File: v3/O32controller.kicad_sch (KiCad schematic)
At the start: 43 parts, among them J1 BATT+, J2 BATT+, J3 BATT-, J4 BATT-, J5 NTC, J6 SWD, J7 ExternalSPI, J8 RS485, J9 RS485, U1 STSPIN32F0ATR, U2 THVD1420DRLR, U3 MA702GQ-P

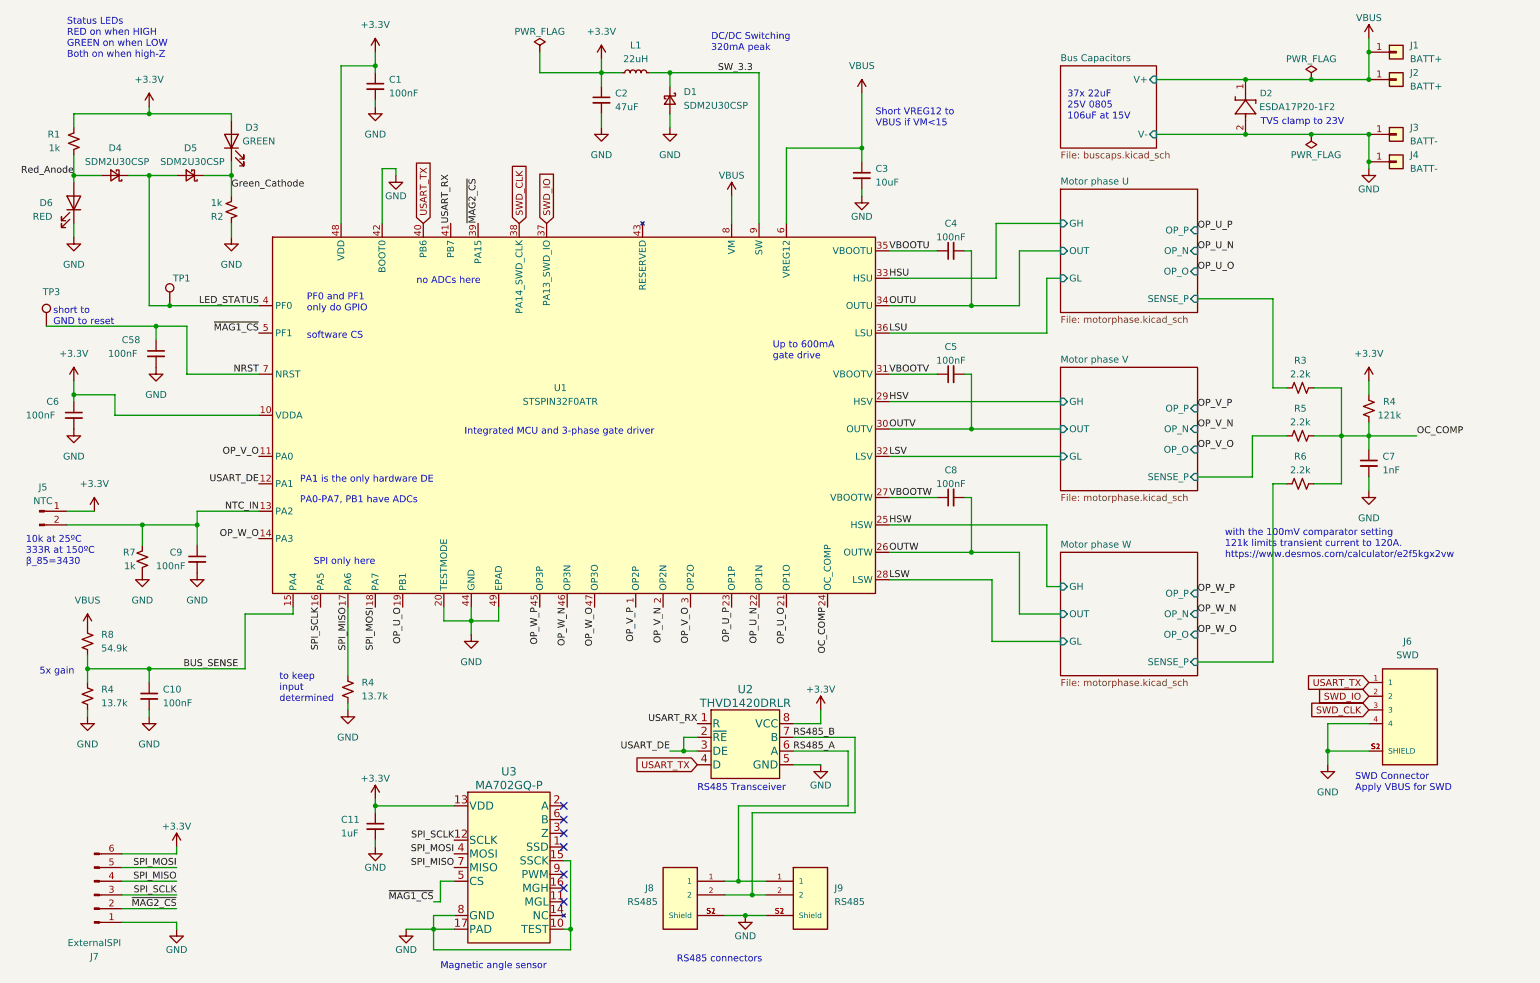
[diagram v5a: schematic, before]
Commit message: use MA732 instead of 702, SMF15A
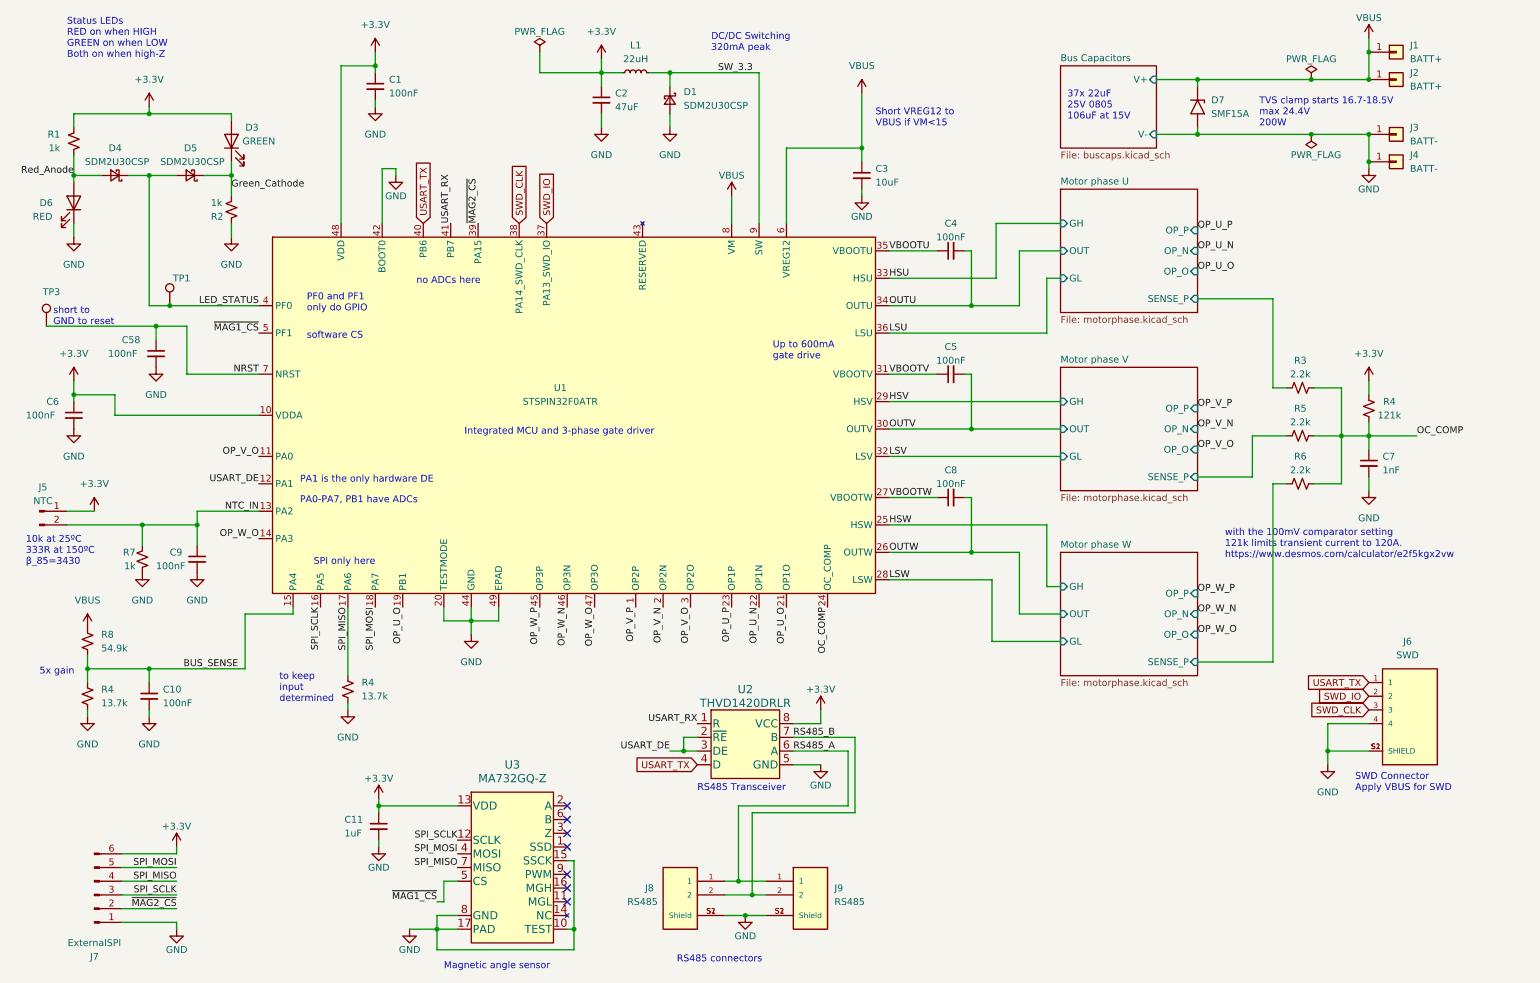
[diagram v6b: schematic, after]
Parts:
- removed D2: ESDA17P20-1F2, O32controller:SMT2_0P91X0P63_STM-L, symbol O32controller:ESDA17P20-1F2
- removed U3: MA702GQ-P, O32controller:MA702GQ-P, symbol O32controller:MA702GQ-P
- added D7: SMF15A, Diode_SMD:D_SMF, symbol Diode:SMF15A
- added U3: MA732GQ-Z, O32controller:QFN-16_MA732, symbol O32controller:MA732GQ-Z
- C1, C10, C4, C5, C58, C6, C8, C9: LCSC (none) -> C100072
- C11: LCSC (none) -> C126521
- C2: LCSC (none) -> C140782
- C3: LCSC (none) -> C194427
- C7: LCSC (none) -> C527029
- D1, D4, D5: LCSC (none) -> C3001723
- D3: LCSC (none) -> C125098
- D6: LCSC (none) -> C125099
- J6: LCSC (none) -> C160404
- J8, J9: LCSC (none) -> C160402
- L1: LCSC (none) -> C2044426
- R1, R2, R7: LCSC (none) -> C106235
- R3, R5, R6: LCSC (none) -> C114762
- R4: LCSC (none) -> C4153138
- R4: LCSC (none) -> C274888
- R8: LCSC (none) -> C137959
- U1: LCSC (none) -> C2651733
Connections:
- net +3.3V: now also U3.13 (VDD)
- net GND: now also D7.2 (A2), U3.10 (TEST), U3.15 (SSCK), U3.17 (PAD), U3.8 (GND)
- net SPI_MISO: now also U3.7 (MISO)
- net SPI_MOSI: now also U3.4 (MOSI)
- net SPI_SCLK: now also U3.12 (SCLK)
- net VBUS: now also D7.1 (A1)
- net ~{MAG1_CS}: now also U3.5 (CS)
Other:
- note added: "TVS clamp starts 16.7-18.5V max 24.4V 200W"
- note removed: "TVS clamp to 23V"
- moved on the sheet: C11

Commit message: finalize BOM for v3.1, shared w Axlab
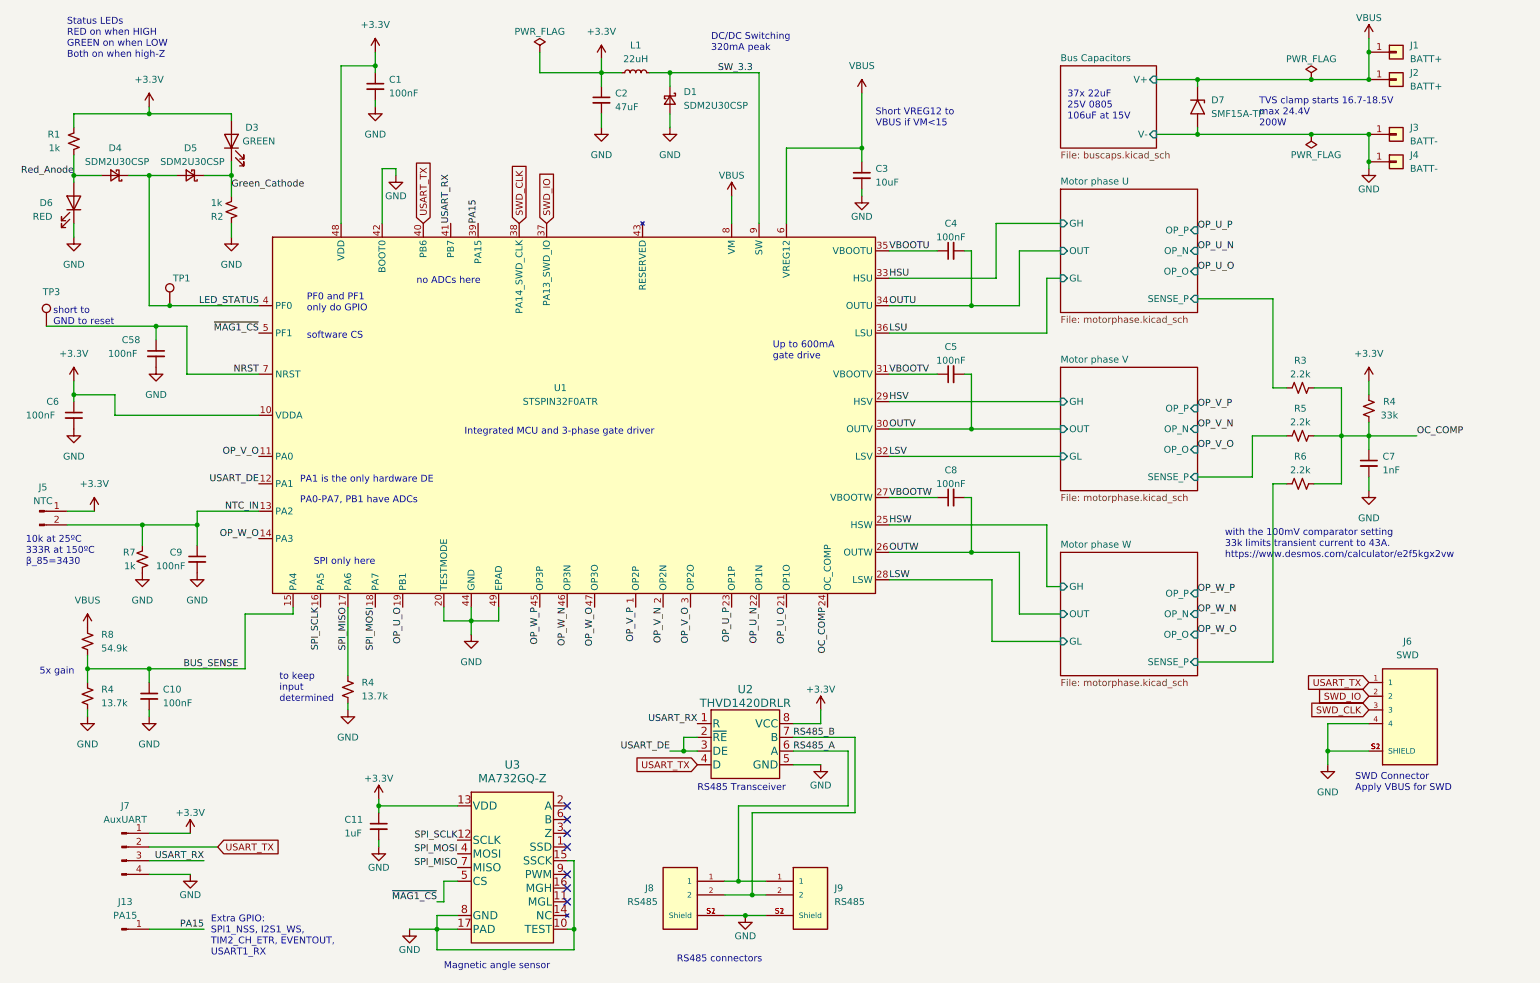
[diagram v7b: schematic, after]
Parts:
- removed J7: ExternalSPI, O32controller:FFC_0.5mm_6p, symbol Connector:Conn_01x06_Pin
- added J13: PA15, O32controller:SolderPad1-1.27mm, symbol Connector:Conn_01x01_Pin
- added J7: AuxUART, O32controller:SolderUART-1.27mm, symbol Connector:Conn_01x04_Pin
- C1, C10, C4, C5, C58, C6, C8, C9: LCSC C100072 -> C307331; MPN CL05A104KA5NNNC -> CL05B104KB54PNC; Type (none) -> Basic; Vendor# C100072 -> C307331
- C11: LCSC C126521 -> C52923; MPN GCM155C71A105KE38D -> CL05A105KA5NQNC; Type (none) -> Basic; Vendor# C126521 -> C52923
- C2, C3, D3, J8, J9, L1, R4, R8, U1: Type (none) -> Extended
- C7: LCSC C527029 -> C1523; MPN CC0402MRX7R9BB102 -> 0402B102K500NT; Type (none) -> Basic; Vendor# C527029 -> C1523
- D1, D4, D5: LCSC C3001723 -> (none); Type (none) -> Global; Vendor LCSC -> Mouser; Vendor# C3001723 -> 621-SDM2U30CSP-7
- D6: LCSC C125099 -> C2286; MPN LTST-C191KRKT -> KT-0603R; Type (none) -> Basic; Vendor# C125099 -> C2286
- D7: value SMF15A -> SMF15A-TP; LCSC (none) -> C914420; MPN (none) -> SMF15A-TP; Type (none) -> Extended; Vendor (none) -> LCSC; Vendor# (none) -> C914420
- J6: LCSC C160404 -> (none); Type (none) -> Global; Vendor LCSC -> Digikey; Vendor# C160404 -> 455-SM04B-SRSS-TBCT-ND
- R1, R2, R7: LCSC C106235 -> C11702; MPN RC0402FR-071KL -> 0402WGF1001TCE; Type (none) -> Basic; Vendor# C106235 -> C11702
- R3, R5, R6: LCSC C114762 -> C25879; MPN RC0402FR-072K2L -> 0402WGF2201TCE; Type (none) -> Basic; Vendor# C114762 -> C25879
- R4: value 121k -> 33k; LCSC C4153138 -> C25779; MPN AF0402FR-07121KL -> 0402WGF3302TCE; Type (none) -> Basic; Vendor# C4153138 -> C25779
- U2: Type (none) -> Global; Vendor Digikey -> TI; Vendor# 296-THVD1420DRLRCT-ND -> THVD1420DRLR
- U3: MPN (none) -> MA732GQ-Z; Type (none) -> Global; Vendor (none) -> Mouser; Vendor# (none) -> 946-MA732GQ-Z
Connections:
- net +3.3V: now also J7.1 (Pin_1)
- net GND: now also J7.4 (Pin_4)
- net USART_RX: now also J7.3 (Pin_3)
- net USART_TX: now also J7.2 (Pin_2)
- net ~{MAG2_CS} renamed PA15
- net PA15: now also J13.1 (Pin_1)
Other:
- note added: "Extra GPIO: SPI1_NSS, I2S1_WS, TIM2_CH_ETR, EVENTOUT, USART1_RX"
- note added: "with the 100mV comparator setting 33k limits transient current to 43A. https://www.desmos.com/calculator/e2f5kgx2vw"
- note removed: "with the 100mV comparator setting 121k limits transient current to 120A. https://www.desmos.com/calculator/e2f5kgx2vw"
